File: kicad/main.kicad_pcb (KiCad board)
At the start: 2 copper layers, 55 x 45 mm, 38 parts, among them IC2 LM358D, IC3 MC34063AD, J1 22-?-0205-7028, J2 22-?-0205-7028, Q1 IRF840, Q2 BC558, Q3 BC848SMD, Q4 BC848SMD

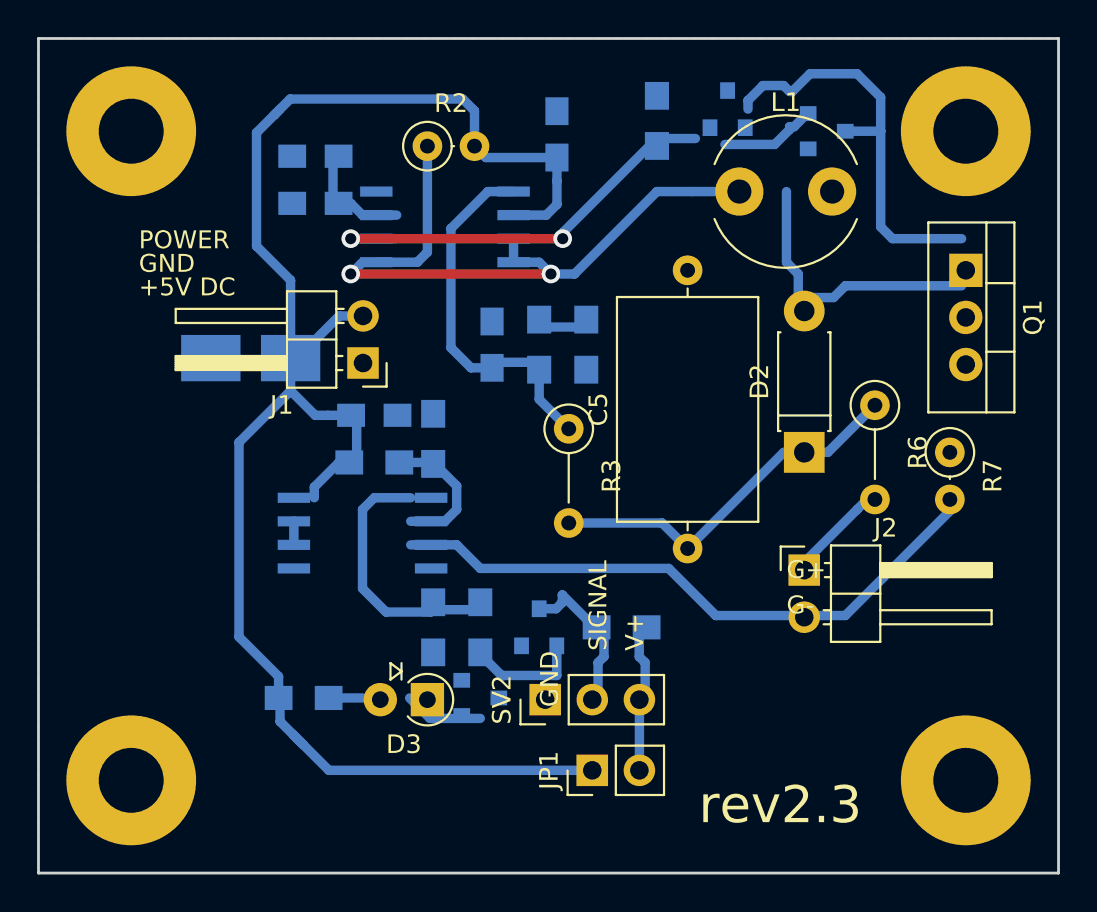
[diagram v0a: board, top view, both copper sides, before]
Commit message: component placement fix
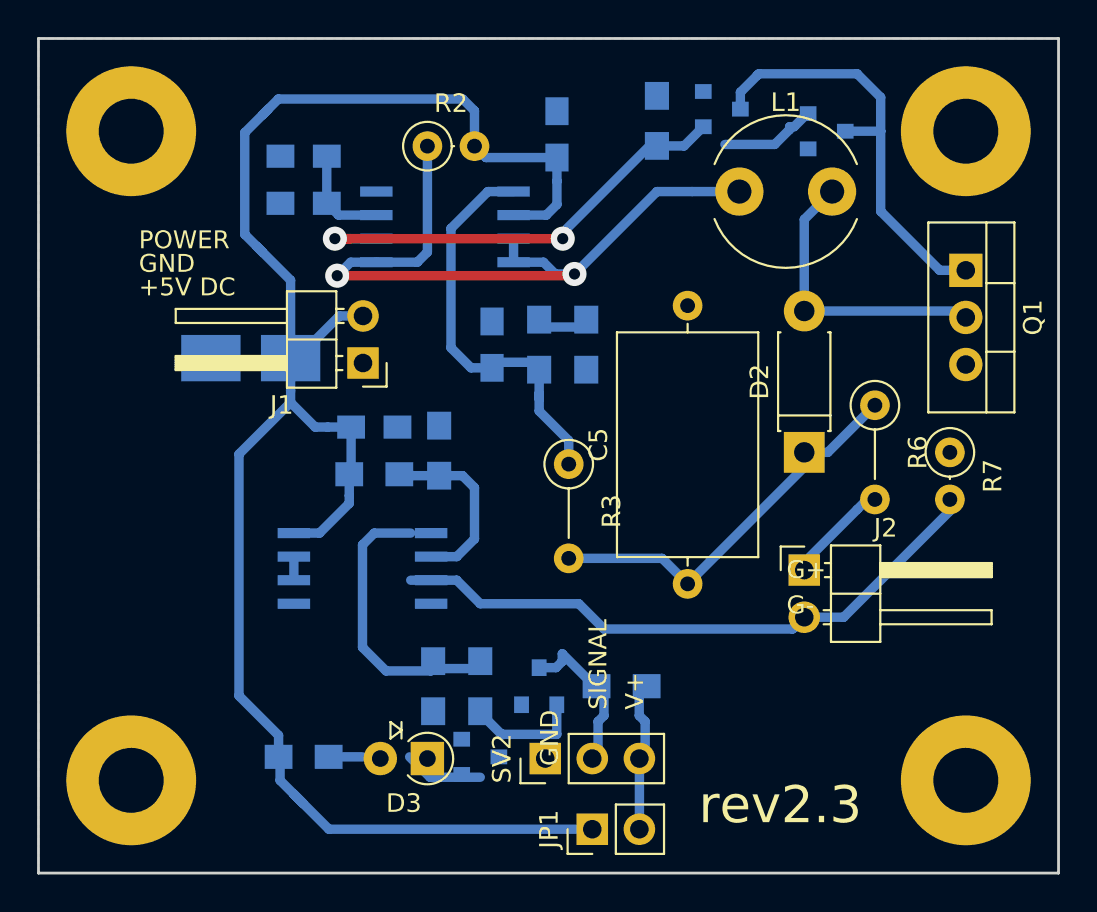
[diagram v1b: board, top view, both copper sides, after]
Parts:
- moved JP1 3.18 mm to (149.9, 127.6)
- moved D3 3.17 mm to (141.0, 123.8)
- moved Q3 3.17 mm to (143.8, 123.7)
- moved Q4 3.17 mm to (147.0, 119.9)
- moved R11 3.17 mm to (141.3, 119.9)
- moved R12 3.17 mm to (143.8, 119.9)
- moved R13 3.17 mm to (134.3, 123.7)
- moved R14 3.17 mm to (151.4, 119.9)
- moved SV2 3.17 mm to (147.3, 123.8)
- moved C5 1.91 mm to (155.0, 114.4)
- moved IC2 1.91 mm to (137.5, 113.6)
- moved R3 1.91 mm to (148.6, 108.0)
- moved R9 0.71 mm to (141.6, 107.2)
- moved R8 0.64 mm to (138.1, 108.5)
- moved C1 0.63 mm to (134.3, 91.3)
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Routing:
- net Net-(C3-Pad1): track 93.2 -> 99.6 mm
- net Net-(IC3-Pad1): track 35.9 -> 39.5 mm
- net Net-(D1-Pad2): track 29.2 -> 31.5 mm
- net Net-(C4-Pad1): track 19.7 -> 21.9 mm
- net Net-(IC2-Pad2): track 8.49 -> 9.85 mm
- net Net-(IC2-Pad1): track 14.0 -> 15.3 mm
- net Net-(C5-Pad1): track 20.3 -> 21.5 mm
- net Net-(D2-Pad2): track 15.1 -> 15.9 mm
- net Net-(D1-Pad1): track 22.5 -> 23.4 mm
- net Net-(C1-Pad1): track 6.24 -> 5.47 mm
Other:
- net class Default: clearance 0.2 -> 0.25; via_dia 0.8 -> 1.3; via_drill 0.4 -> 0.6
- rule trace_clearance: 0.2 -> 0.25

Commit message: elements placement fix
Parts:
- D3: footprint Diodes_THT:D_A-405_P2.54mm_Vertical_AnodeUp -> LEDs:LED_D3.0mm
- J1: value 22-?-0205-7028 -> Power
- J2: value 22-?-0205-7028 -> GM Tube
- Q2: value BC558 -> BC808
- R14: value R-EU_M0805 -> 1k
- R4: value 30k+1k -> 1k
- R5: value 30k+1k -> 30k
- R8: value R-EU_R0805 -> ?
- SV2: value MA03-1 -> Digital Output
- moved JP1 9.09 mm to (141.0, 125.7)
- moved D3 6.35 mm to (134.6, 123.8), turned to 90 degrees
- moved Q3 6.29 mm to (137.8, 121.9), turned to 180 degrees
- moved R13 5.23 mm to (132.7, 118.7)
- moved SV2 2.29 mm to (148.6, 125.7)
- moved Q2 1.30 mm to (161.3, 89.5)
- turned Q4 to 0 degrees
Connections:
- Q2 pad 1: GND -> Net-(D1-Pad2)
- Q2 pad 2: Net-(D1-Pad2) -> Net-(D1-Pad1)
- Q2 pad 3: Net-(D1-Pad1) -> GND
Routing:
- net Net-(C3-Pad1): track 99.6 -> 83.9 mm
- net Net-(JP1-Pad2): track 7.75 -> 18.7 mm
- net Net-(D1-Pad2): track 31.5 -> 26.3 mm
- net Net-(Q4-Pad1): track 6.31 -> 2.44 mm
- net Net-(D3-Pad1): track 0.00 -> 2.96 mm
- net Net-(D1-Pad1): track 23.4 -> 21.5 mm
- net Net-(Q3-Pad1): track 4.59 -> 2.93 mm
- net Net-(D3-Pad2): track 2.22 -> 2.77 mm
- net GND: vias 0 -> 7

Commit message: drc check ok
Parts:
- Q2: value BC808 -> Q_PNP_BEC
- moved D1 1.27 mm to (155.6, 88.8)
- moved L1 1.27 mm to (156.5, 93.3)
- moved R1 1.27 mm to (152.1, 89.4)
- moved Q2 1.27 mm to (160.0, 89.5)
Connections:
- Q2 pad 2: Net-(D1-Pad1) -> GND
- Q2 pad 3: GND -> Net-(D1-Pad1)
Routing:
- net Net-(D1-Pad1): track 21.5 -> 28.7 mm
- net Net-(D1-Pad2): track 26.3 -> 30.4 mm
- net Net-(IC3-Pad1): track 39.5 -> 38.2 mm
- net Net-(IC2-Pad3): track 32.9 -> 31.8 mm
- net Net-(IC2-Pad1): track 15.3 -> 16.4 mm
- net Net-(D2-Pad2): track 15.9 -> 15.4 mm
- net GND: vias 7 -> 8
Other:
- board text removed: "POWER"
